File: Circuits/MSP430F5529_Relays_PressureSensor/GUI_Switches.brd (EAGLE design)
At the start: 123.8 x 90.5 mm, 7 parts

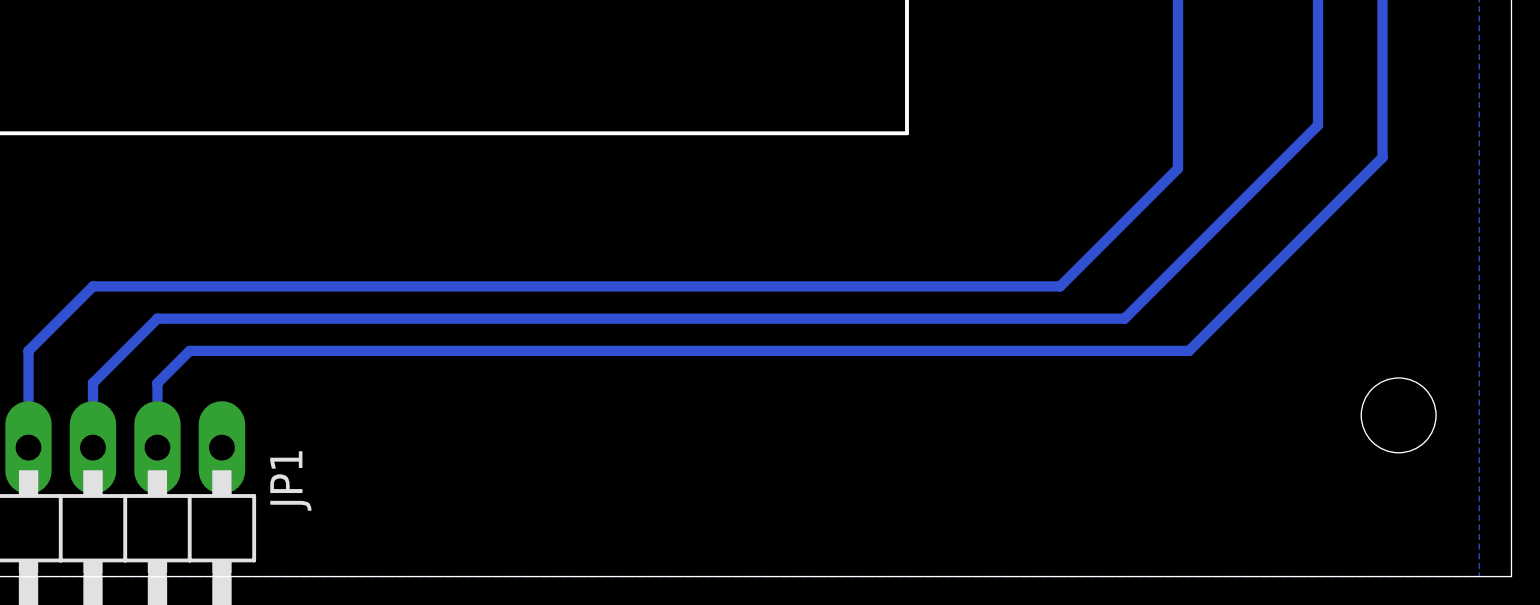
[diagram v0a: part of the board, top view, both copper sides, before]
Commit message: Add power supply and connector for GUI_Switches board
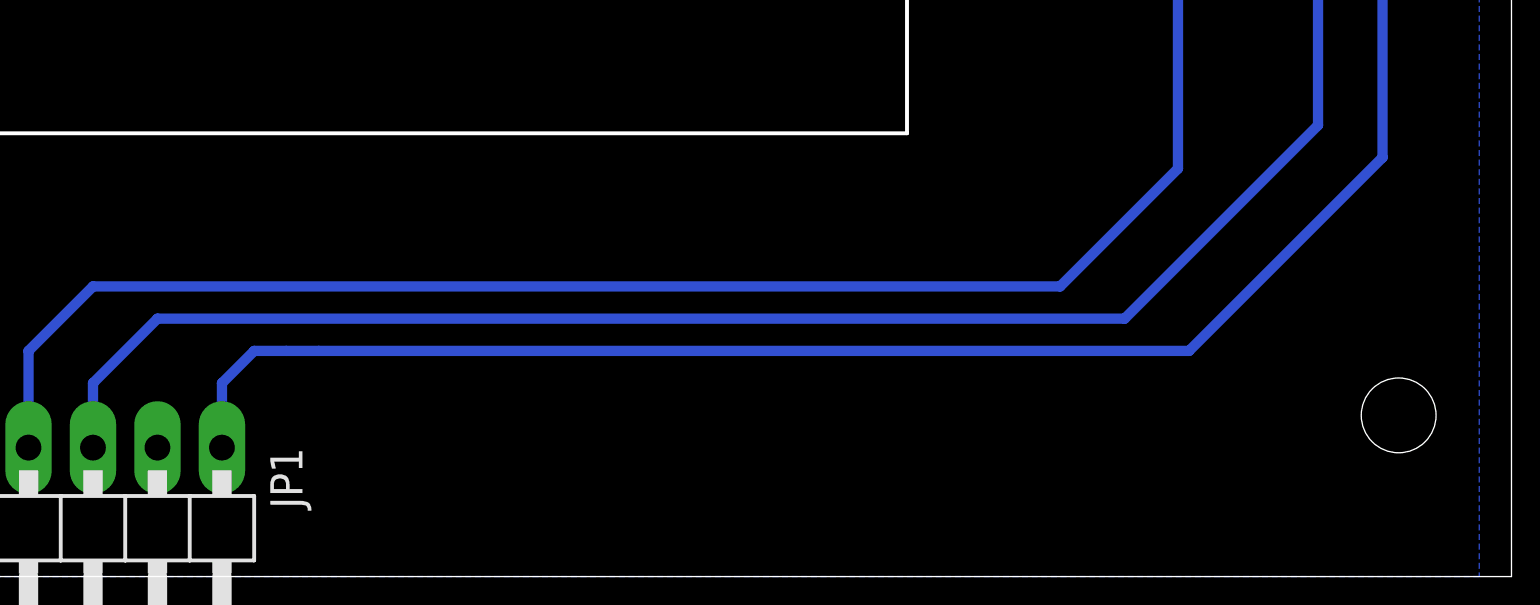
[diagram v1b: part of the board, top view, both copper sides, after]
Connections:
- net GND: now also JP1.2; no longer JP1.1
- net N$6: now also JP1.1; no longer JP1.2
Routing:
- net N$6: track 106.8 -> 104.3 mm
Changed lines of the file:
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@@
 <contactref element="S_UR" pad="1"/>
 <contactref element="JP1" pad="5"/>
-<contactref element="JP1" pad="1"/>
 <contactref element="JP1" pad="6"/>
 <contactref element="JP1" pad="10"/>
+<contactref element="JP1" pad="2"/>
 </signal>
 <signal name="N$1">
@@
 <signal name="N$6">
 <contactref element="S_UR" pad="2"/>
-<contactref element="JP1" pad="2"/>
-<wire x1="73.66" y1="-1.27" x2="73.66" y2="1.27" width="0.4064" layer="16"/>
-<wire x1="73.66" y1="1.27" x2="74.93" y2="2.54" width="0.4064" layer="16"/>
 <wire x1="119.28" y1="55.98" x2="113.8625" y2="55.98" width="0.4064" layer="16"/>
 <wire x1="121.92" y1="10.16" x2="121.92" y2="53.34" width="0.4064" layer="16"/>
 <wire x1="121.92" y1="53.34" x2="119.28" y2="55.98" width="0.4064" layer="16"/>
-<wire x1="74.93" y1="2.54" x2="114.3" y2="2.54" width="0.4064" layer="16"/>
-<wire x1="114.3" y1="2.54" x2="121.92" y2="10.16" width="0.4064" layer="16"/>
+<wire x1="121.92" y1="10.16" x2="114.3" y2="2.54" width="0.4064" layer="16"/>
+<contactref element="JP1" pad="1"/>
+<wire x1="114.3" y1="2.54" x2="80.01" y2="2.54" width="0.4064" layer="16"/>
+<wire x1="80.01" y1="2.54" x2="78.74" y2="2.54" width="0.4064" layer="16"/>
+<wire x1="76.2" y1="-1.27" x2="76.2" y2="1.27" width="0.4064" layer="16"/>
+<wire x1="76.2" y1="1.27" x2="77.47" y2="2.54" width="0.4064" layer="16"/>
+<wire x1="77.47" y1="2.54" x2="78.74" y2="2.54" width="0.4064" layer="16"/>
 </signal>
 <signal name="N$7">
